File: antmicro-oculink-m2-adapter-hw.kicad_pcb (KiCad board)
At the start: 4 copper layers, 0 parts

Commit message: [#79281] Add ci.yml, initial connector placement
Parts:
- added J1: OCuLink_x4_Amphenol_G14A421211112HR, antmicro-footprints:Amphenol_G14A421211112HR, F.Cu at (146.2, 103.1)
- added J2: PCB-Edge_M.2_Key-M, antmicro-footprints:PCB-Edge_M.2_Key-M, F.Cu at (146.3, 130.6)
- added REF**: LOGO, antmicro-footprints:antmicro-logo_scaled_12mm, F.Cu at (146.1, 93.5)
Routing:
- net /PCIe_{REF0}.CK-: track 0.00 -> 1.08 mm
- net /PCIe_{REF0}.CK+: track 0.00 -> 1.08 mm
- net GND: vias 0 -> 3
- added copper zone on In1.Cu, net GND
- added copper zone on In2.Cu, net GND
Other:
- board outline added: 22 x 76 mm

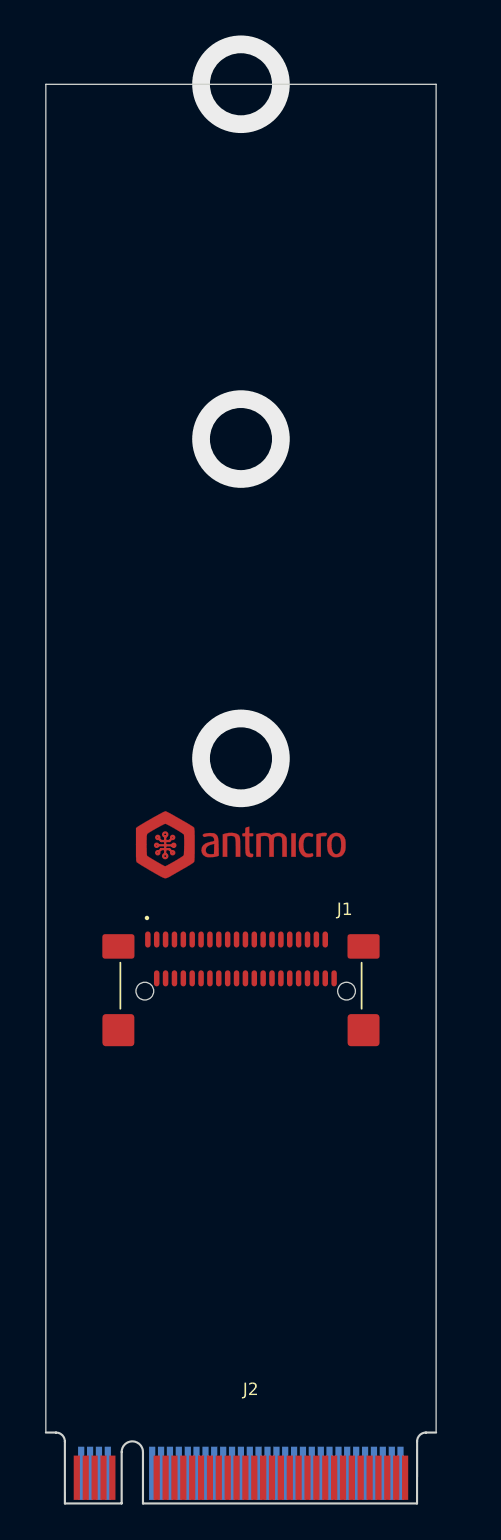
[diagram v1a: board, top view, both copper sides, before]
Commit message: [#79281] Connector placement and PCIe routing
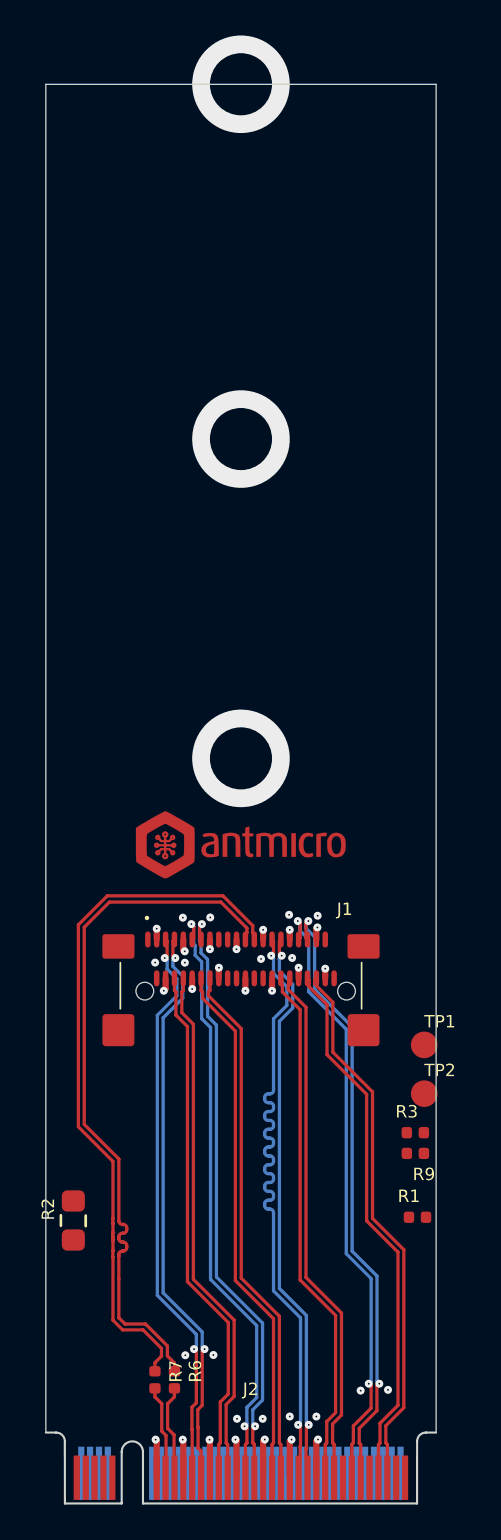
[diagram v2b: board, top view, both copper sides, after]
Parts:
- added R1: R_0R_0402, antmicro-footprints:R_0402_1005Metric, F.Cu at (156.1, 114.5)
- added R2: R_0R_0805, antmicro-footprints:R_0805_2012Metric, F.Cu at (136.7, 114.7)
- added R3: R_0R_0402, antmicro-footprints:R_0402_1005Metric, F.Cu at (156.0, 109.7)
- added R6: R_0R_0402, antmicro-footprints:R_0402_1005Metric, F.Cu at (142.4, 123.6)
- added R7: R_0R_0402, antmicro-footprints:R_0402_1005Metric, F.Cu at (141.3, 123.6)
- added R9: R_0R_0402, antmicro-footprints:R_0402_1005Metric, F.Cu at (156.0, 110.9)
- added TP1: TP_1.5mm_SMD, antmicro-footprints:TP_SMD_1.5mm, F.Cu at (156.5, 104.8)
- added TP2: TP_1.5mm_SMD, antmicro-footprints:TP_SMD_1.5mm, F.Cu at (156.5, 107.5)
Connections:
- J1 pad B12: /PCIe_{REF0}_R.CK+ -> /PCIe_{REF0}_R.CK-
- J1 pad B13: /PCIe_{REF0}_R.CK- -> /PCIe_{REF0}_R.CK+
- J2 pad 23: /PCIe_{x4}.RX2+ -> /PCIe_{x4}.RX2-
- J2 pad 25: /PCIe_{x4}.RX2- -> /PCIe_{x4}.RX2+
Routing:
- net /PCIe_{REF0}_R.CK+: track 0.00 -> 40.0 mm
- net /PCIe_{REF0}_R.CK-: track 0.00 -> 39.9 mm
- net /PCIe_{x4}.RX2+: track 0.00 -> 36.3 mm, vias 0 -> 2
- net /PCIe_{x4}.RX3-: track 0.00 -> 34.8 mm, vias 0 -> 2
- net /PCIe_{x4}.RX3+: track 0.00 -> 34.8 mm, vias 0 -> 2
- net /PCIe_{x4}.RX1+: track 0.00 -> 34.1 mm, vias 0 -> 2
- net /PCIe_{x4}.RX1-: track 0.00 -> 34.1 mm, vias 0 -> 2
- net /PCIe_{x4}.RX0-: track 0.00 -> 32.4 mm, vias 0 -> 2
- net /PCIe_{x4}.RX0+: track 0.00 -> 32.3 mm, vias 0 -> 2
- net /PCIe_{x4}.RX2-: track 0.00 -> 31.9 mm, vias 0 -> 2
- net /PCIe_{x4}.TX3+: track 0.00 -> 30.7 mm
- net /PCIe_{x4}.TX3-: track 0.00 -> 30.7 mm
- net /PCIe_{x4}.TX1-: track 0.00 -> 29.9 mm
- net /PCIe_{x4}.TX1+: track 0.00 -> 29.9 mm
- net /PCIe_{x4}.TX2-: track 0.00 -> 29.7 mm
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
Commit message: [#79281] Clean up gnd vias and pcie routing
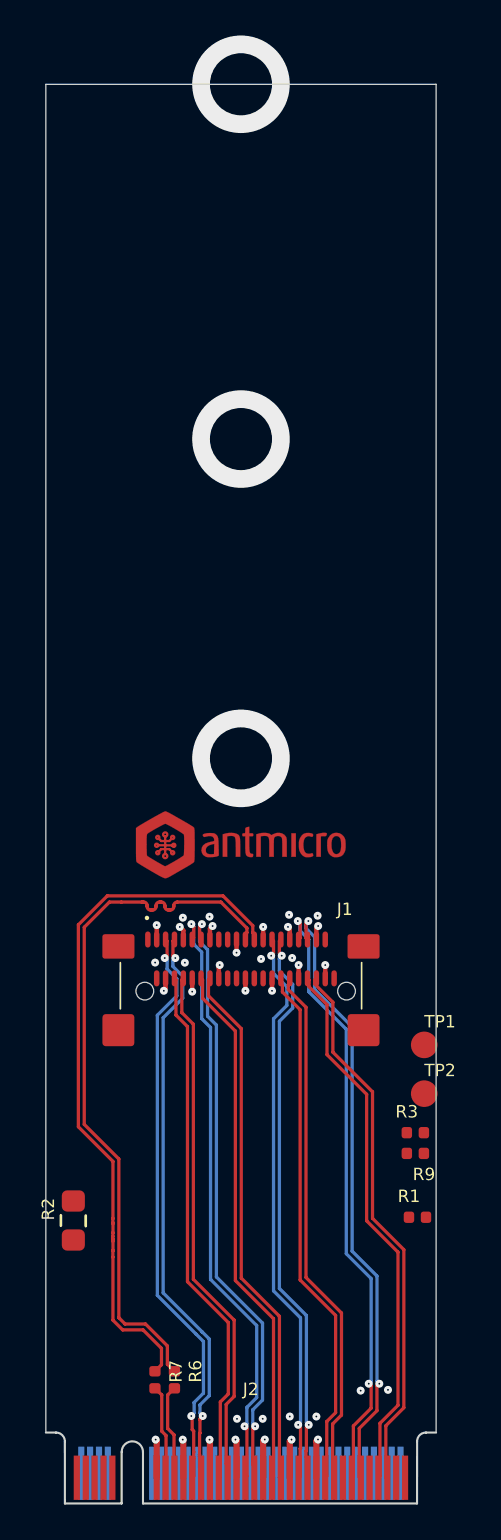
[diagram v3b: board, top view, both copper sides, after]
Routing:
- net /PCIe_{x4}.RX2+: track 36.3 -> 32.9 mm
- net GND: track 23.9 -> 25.8 mm, vias 40 -> 38
